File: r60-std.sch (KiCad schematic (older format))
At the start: 147 parts, among them K0 ESC, K0A1 0, K0B1 MINUS, K0C1 EQUAL, K0D1 BACKSP, K1 1, K10 TAB, K11 Q, K12 W, K13 E, K14 R, K15 T, K16 Y, K17 U, K18 I, K19 O, K1A1 P, K1B1 LBRACE, K1C1 RBRACE, K1D1 BS_PIPE, K2 2, K20 CAPS, K20-S1 CAPS, K21 A, K22 S, K23 D, K24 F, K25 G, K26 H, K27 J, K28 K, K29 L, K2A1 COLON, K2B1 QUOTE, K2D1 ENTER, K3 3, K30 LSHIFT, K31 Z, K32 x, K33 C, K34 V, K35 B, K36 N, K37 M, K38 COMMA, K39 DOT, K3A1 SLASH, K3B1 RSHIFT, K4 4, K40 LCTL, K41 LWIN, K42 LALT, K43 LFN, K44 SSPACE-1, K45 SPACE, K45-1 SSPACE-2, K48 RALT, K49 RWIN, K4A1 RGUI, K4B1 RCTL, K5 5, K6 6, K7 7, K8 8, K9 9, P1 USB_B, SW1 SW_Push, U1 ATmega32U4-AU, Y1 16MHz

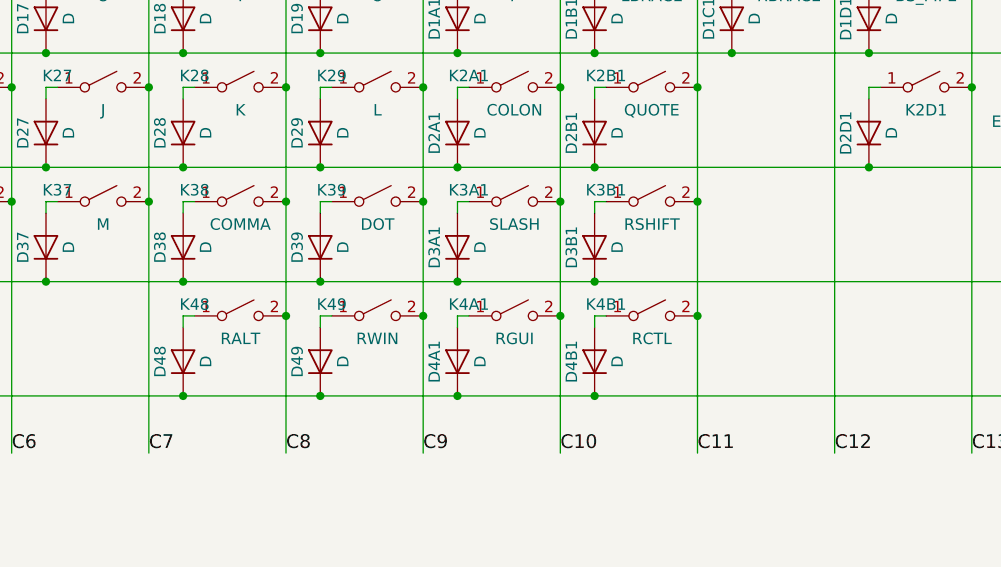
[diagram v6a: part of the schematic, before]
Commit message: add option for split right shift
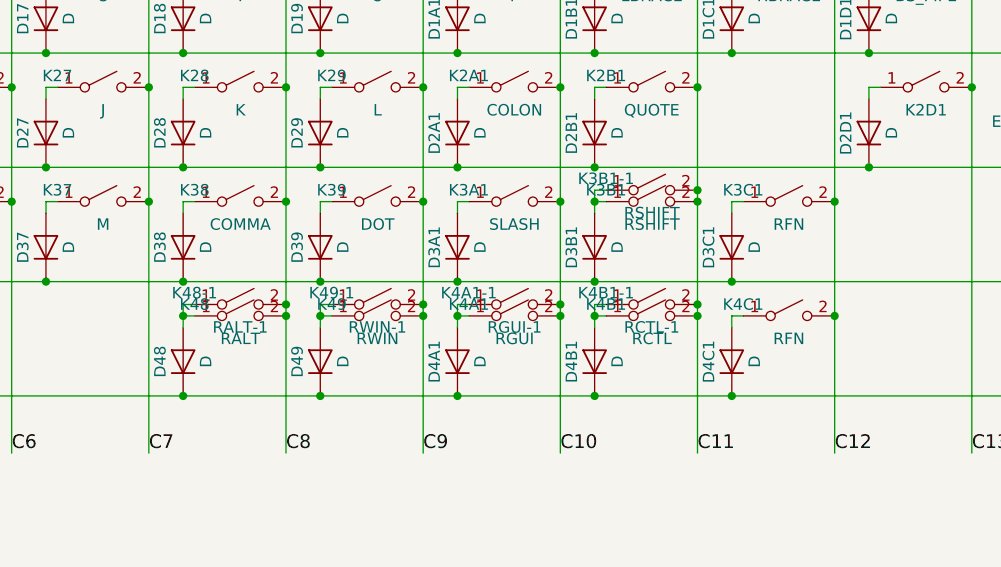
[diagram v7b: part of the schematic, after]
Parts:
- added D3C1, D4C1: D, Keyboard:D_0805, symbol D
- added K3B1-1: RSHIFT, Keyboard:CHERRY_PCB_175H, symbol SW_SPST
- added K3C1, K4C1: RFN, Keyboard:CHERRY_PCB_100H, symbol SW_SPST
- added K48-1: RALT-1, Keyboard:CHERRY_PCB_100H, symbol SW_SPST
- added K49-1: RWIN-1, Keyboard:CHERRY_PCB_100H, symbol SW_SPST
- added K4A1-1: RGUI-1, Keyboard:CHERRY_PCB_100H, symbol SW_SPST
- added K4B1-1: RCTL-1, Keyboard:CHERRY_PCB_100H, symbol SW_SPST
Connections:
- wire segments 230 -> 239
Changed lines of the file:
@@
 	7650 2450 7600 2450
 Wire Wire Line
-	7600 2450 7600 2500
+	7600 2400 7600 2500
 Wire Wire Line
 	1050 2950 1000 2950
@@
 	5850 2950 5800 2950
 Wire Wire Line
-	5800 2950 5800 3000
+	5800 2900 5800 3000
 Wire Wire Line
 	6450 2950 6400 2950
 Wire Wire Line
-	6400 2950 6400 3000
+	6400 2900 6400 3000
 Wire Wire Line
 	7050 2950 7000 2950
 Wire Wire Line
-	7000 2950 7000 3000
+	7000 2900 7000 3000
 Wire Wire Line
 	7650 2950 7600 2950
 Wire Wire Line
-	7600 2950 7600 3000
+	7600 2900 7600 3000
 Wire Wire Line
 	9250 950  9250 3550
@@
 	1    0    0    -1
 $EndComp
+$Comp
+L SW_SPST K48-1
+U 1 1 5AF14BF5
+P 6050 2900
+F 0 "K48-1" H 5850 2950 50  0000 C CNN
+F 1 "RALT-1" H 6050 2800 50  0000 C CNN
+F 2 "Keyboard:CHERRY_PCB_100H" H 6050 2900 50  0001 C CNN
+F 3 "" H 6050 2900 50  0000 C CNN
+	1    6050 2900
+	1    0    0    -1
+$EndComp
+$Comp
+L SW_SPST K49-1
+U 1 1 5AF14DBF
+P 6650 2900
+F 0 "K49-1" H 6450 2950 50  0000 C CNN
+F 1 "RWIN-1" H 6650 2800 50  0000 C CNN
+F 2 "Keyboard:CHERRY_PCB_100H" H 6650 2900 50  0001 C CNN
+F 3 "" H 6650 2900 50  0000 C CNN
+	1    6650 2900
+	1    0    0    -1
+$EndComp
+$Comp
+L SW_SPST K4A1-1
+U 1 1 5AF14F90
+P 7250 2900
+F 0 "K4A1-1" H 7050 2950 50  0000 C CNN
+F 1 "RGUI-1" H 7250 2800 50  0000 C CNN
+F 2 "Keyboard:CHERRY_PCB_100H" H 7250 2900 50  0001 C CNN
+F 3 "" H 7250 2900 50  0000 C CNN
+	1    7250 2900
+	1    0    0    -1
+$EndComp
+$Comp
+L SW_SPST K4B1-1
+U 1 1 5AF15164
+P 7850 2900
+F 0 "K4B1-1" H 7650 2950 50  0000 C CNN
+F 1 "RCTL-1" H 7850 2800 50  0000 C CNN
+F 2 "Keyboard:CHERRY_PCB_100H" H 7850 2900 50  0001 C CNN
+F 3 "" H 7850 2900 50  0000 C CNN
+	1    7850 2900
+	1    0    0    -1
+$EndComp
+Connection ~ 6250 2900
+Wire Wire Line
+	5850 2900 5800 2900
+Connection ~ 5800 2950
+Wire Wire Line
+	6450 2900 6400 2900
+Connection ~ 6400 2950
+Connection ~ 6850 2900
+Wire Wire Line
+	7050 2900 7000 2900
+Connection ~ 7000 2950
+Connection ~ 7450 2900
+Wire Wire Line
+	7650 2900 7600 2900
+Connection ~ 7600 2950
+Connection ~ 8050 2900
+$Comp
+L D D4C1
+U 1 1 5AF2213F
+P 8200 3150
+F 0 "D4C1" H 8200 3250 50  0000 C CNN
+F 1 "D" H 8200 3050 50  0000 C CNN
+F 2 "Keyboard:D_0805" H 8200 3150 50  0001 C CNN
+F 3 "" H 8200 3150 50  0000 C CNN
+	1    8200 3150
+	0    -1   -1   0
+$EndComp
+$Comp
+L SW_SPST K4C1
+U 1 1 5AF2259B
+P 8450 2950
+F 0 "K4C1" H 8250 3000 50  0000 C CNN
+F 1 "RFN" H 8450 2850 50  0000 C CNN
+F 2 "Keyboard:CHERRY_PCB_100H" H 8450 2950 50  0001 C CNN
+F 3 "" H 8450 2950 50  0000 C CNN
+	1    8450 2950
+	1    0    0    -1
+$EndComp
+Wire Wire Line
+	8250 2950 8200 2950
+Wire Wire Line
+	8200 2950 8200 3000
+Connection ~ 8650 2950
+Connection ~ 8200 3300
+$Comp
+L SW_SPST K3C1
+U 1 1 5AF3B594
+P 8450 2450
+F 0 "K3C1" H 8250 2500 50  0000 C CNN
+F 1 "RFN" H 8450 2350 50  0000 C CNN
+F 2 "Keyboard:CHERRY_PCB_100H" H 8450 2450 50  0001 C CNN
+F 3 "" H 8450 2450 50  0000 C CNN
+	1    8450 2450
+	1    0    0    -1
+$EndComp
+$Comp
+L D D3C1
+U 1 1 5AF3FE8F
+P 8200 2650
+F 0 "D3C1" H 8200 2750 50  0000 C CNN
+F 1 "D" H 8200 2550 50  0000 C CNN
+F 2 "Keyboard:D_0805" H 8200 2650 50  0001 C CNN
+F 3 "" H 8200 2650 50  0000 C CNN
+	1    8200 2650
+	0    -1   -1   0
+$EndComp
+Wire Wire Line
+	8250 2450 8200 2450
+Wire Wire Line
+	8200 2450 8200 2500
+Connection ~ 8650 2450
+Connection ~ 8200 2800
+$Comp
+L SW_SPST K3B1-1
+U 1 1 5AF4529F
+P 7850 2400
+F 0 "K3B1-1" H 7650 2450 50  0000 C CNN
+F 1 "RSHIFT" H 7850 2300 50  0000 C CNN
+F 2 "Keyboard:CHERRY_PCB_175H" H 7850 2400 50  0001 C CNN
+F 3 "" H 7850 2400 50  0000 C CNN
+	1    7850 2400
+	1    0    0    -1
+$EndComp
+Wire Wire Line
+	7650 2400 7600 2400
+Connection ~ 7600 2450
+Connection ~ 8050 2400
 $EndSCHEMATC
